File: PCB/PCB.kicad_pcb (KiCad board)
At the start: 2 copper layers, 120 x 60 mm, 63 parts, among them J1 USB_C_Receptacle_USB2.0_16P, J2 Conn_01x15, J3 Conn_01x15, Q2 IRLML2060, SW1 TSA016A2526B, SW2 TSA016A2526B, SW3 TSA016A2526B, U1 RP2040, U2 USBLC6-2SC6, U3 NCP1117ST33T3G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

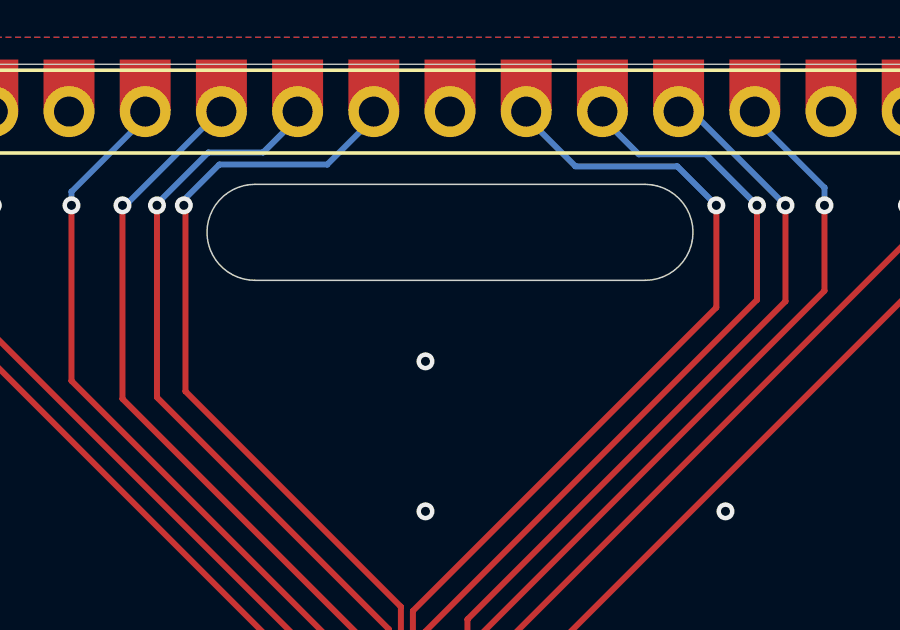
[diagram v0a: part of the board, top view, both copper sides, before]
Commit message: new mounting hole
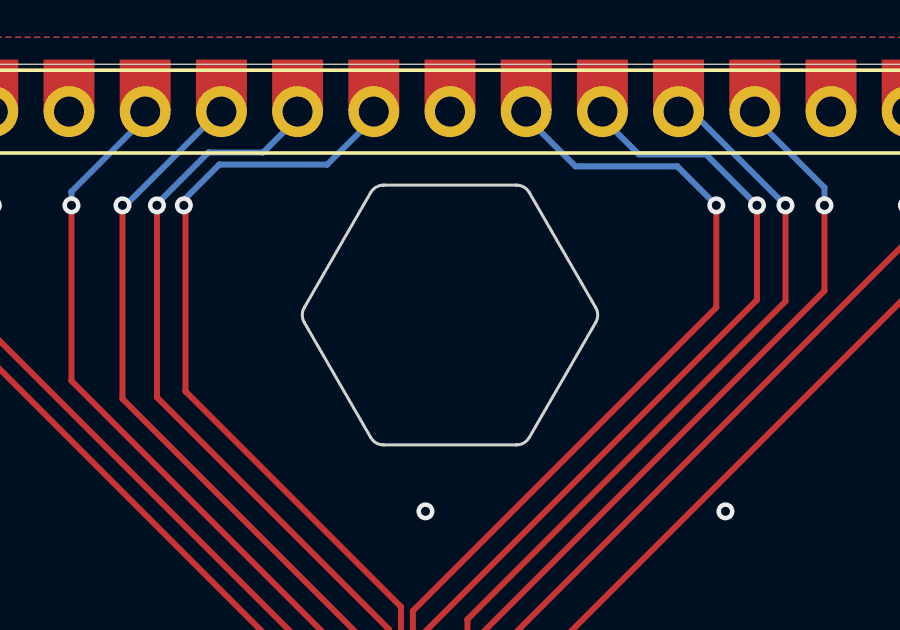
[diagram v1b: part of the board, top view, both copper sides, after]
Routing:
- net GND: vias 112 -> 111
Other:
- outline, holes or cut-outs redrawn
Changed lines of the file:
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@@
 			)
 		)
+		(model "/home/kai/Downloads/2-9in-e-ink-display-red-black-1.snapshot.11/Waveshare 2.9 (B) E-ink - Display Folded Flush.stp"
+			(offset
+				(xyz 0 28 1.5)
+			)
+			(scale
+				(xyz 1 1 1)
+			)
+			(rotate
+				(xyz -0 -0 -90)
+			)
+		)
 	)
 	(footprint "Capacitor_SMD:C_0402_1005Metric"
@@
 		(layer "Dwgs.User")
 	)
-	(gr_arc
-		(start 147.317629 29.1)
-		(mid 148.9176 30.7)
-		(end 147.317629 32.3)
+	(gr_line
+		(start 138.173261 29.374999)
+		(end 135.961936 33.205129)
 		(stroke
-			(width 0.05)
+			(width 0.1)
 			(type default)
 		)
@@
 		(layer "Edge.Cuts")
 	)
+	(gr_arc
+		(start 138.173261 29.374999)
+		(mid 138.356274 29.191987)
+		(end 138.606273 29.125)
+		(stroke
+			(width 0.1)
+			(type default)
+		)
+		(layer "Edge.Cuts")
+	)
 	(gr_line
-		(start 134.317629 32.3)
-		(end 147.317629 32.3)
+		(start 138.606273 37.785254)
+		(end 143.028909 37.785254)
 		(stroke
-			(width 0.05)
+			(width 0.1)
 			(type default)
 		)
@@
 	)
 	(gr_arc
+		(start 135.961936 33.705125)
+		(mid 135.894949 33.455127)
+		(end 135.961936 33.205129)
+		(stroke
+			(width 0.1)
+			(type default)
+		)
+		(layer "Edge.Cuts")
+	)
+	(gr_arc
+		(start 145.673265 33.205134)
+		(mid 145.740251 33.45513)
+		(end 145.673262 33.705125)
+		(stroke
+			(width 0.1)
+			(type default)
+		)
+		(layer "Edge.Cuts")
+	)
+	(gr_arc
+		(start 138.606273 37.785254)
+		(mid 138.356273 37.718267)
+		(end 138.173261 37.535254)
+		(stroke
+			(width 0.1)
+			(type default)
+		)
+		(layer "Edge.Cuts")
+	)
+	(gr_arc
 		(start 192.55414 85.097818)
 		(mid 192.210306 84.96078)
@@
 		(layer "Edge.Cuts")
 	)
+	(gr_line
+		(start 143.028939 29.125)
+		(end 138.606273 29.125)
+		(stroke
+			(width 0.1)
+			(type default)
+		)
+		(layer "Edge.Cuts")
+	)
+	(gr_arc
+		(start 143.461944 37.535243)
+		(mid 143.278922 37.718265)
+		(end 143.028909 37.785254)
+		(stroke
+			(width 0.1)
+			(type default)
+		)
+		(layer "Edge.Cuts")
+	)
+	(gr_line
+		(start 143.461944 37.535243)
+		(end 145.673262 33.705125)
+		(stroke
+			(width 0.1)
+			(type default)
+		)
+		(layer "Edge.Cuts")
+	)
 	(gr_arc
 		(start 192.054848 25.570791)
@@
 	)
 	(gr_line
-		(start 192.558935 25.097818)
-		(end 209.08114 25.097818)
+		(start 145.673265 33.205134)
+		(end 143.461932 29.374991)
 		(stroke
-			(width 0.01)
+			(width 0.1)
 			(type default)
 		)
@@
 	)
 	(gr_line
-		(start 192.55414 85.097818)
-		(end 209.08583 85.097818)
+		(start 192.558935 25.097818)
+		(end 209.08114 25.097818)
 		(stroke
 			(width 0.01)
@@
 		(layer "Edge.Cuts")
 	)
-	(gr_arc
-		(start 134.317629 32.3)
-		(mid 132.7176 30.7)
-		(end 134.317629 29.1)
+	(gr_line
+		(start 192.55414 85.097818)
+		(end 209.08583 85.097818)
 		(stroke
-			(width 0.05)
+			(width 0.01)
 			(type default)
 		)
@@
 	)
 	(gr_line
-		(start 147.317629 29.1)
-		(end 134.317629 29.1)
+		(start 135.961936 33.705125)
+		(end 138.173261 37.535254)
 		(stroke
-			(width 0.05)
+			(width 0.1)
 			(type default)
 		)
@@
 		(layer "Edge.Cuts")
 	)
+	(gr_arc
+		(start 143.028939 29.125)
+		(mid 143.278929 29.191985)
+		(end 143.461932 29.374991)
+		(stroke
+			(width 0.1)
+			(type default)
+		)
+		(layer "Edge.Cuts")
+	)
 	(gr_text "Some sketchy ground stuff, but I wanted it symmetrical and also a nice no-fill"
 		(at 186 23 0)
@@
 	)
 	(via
-		(at 140 35)
-		(size 0.6)
-		(drill 0.3)
-		(layers "F.Cu" "B.Cu")
-		(free yes)
-		(net 2)
-	)
-	(via
 		(at 140.65 48.2)
 		(size 0.6)
@@
 	)
 	(group ""
-		(members "162ab123-923f-4e19-be61-0324decd1f67" "1efb17f0-22fb-40ea-8807-f4fe69c3b792"
-			"b7a0f540-713e-4c9b-964d-49741287ba49" "b864c2af-c021-4858-a3a0-57c0e8108585"
+		(members "0ce7d37b-55d1-42f5-b13d-9c9e3b05c39b" "1f2a5adc-6555-4ce7-a0a5-fbe4a5895658"
+			"2173a039-1b9a-4af3-a71f-11988ef09e77" "54306ec1-47c2-4ec0-9eab-b388f6fdc17e"
+			"5c52c278-44df-4e44-92cc-903473877560" "62448e19-7cc3-44b4-a87d-d9a49ac190a5"
+			"762d25f0-1da9-4a48-9eb9-bc840d037b1e" "8121fe78-a763-4337-866c-79c3fbb7839a"
+			"90dd8e04-e499-4d71-acf3-162c82c6a650" "a5d14ade-53ac-40ed-b384-6d3397fe894e"
+			"b7da73b2-b1ba-4571-aaf0-42c2c0c642ad" "f407a7cb-ce11-4b17-9b3c-b1eebdf68950"
 		)
 	)

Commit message: new fab filess with changes
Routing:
- net /GPIO24: track 32.3 -> 27.8 mm
- net /GPIO23: track 33.6 -> 30.1 mm
- net /GPIO25: track 30.9 -> 28.2 mm
- net /GPIO22: track 32.8 -> 30.4 mm
- net /GPIO26: track 29.7 -> 28.6 mm
- net +3V3: track 256.5 -> 255.9 mm
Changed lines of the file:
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@@
 			)
 			(rotate
-				(xyz -0 -0 -90)
+				(xyz -0 -0 90)
 			)
 		)
@@
 	)
 	(segment
+		(start 151.2 29.8)
+		(end 151.2 33.8)
+		(width 0.2)
+		(layer "F.Cu")
+		(net 3)
+	)
+	(segment
 		(start 136.478778 54.340998)
 		(end 135.943504 54.340998)
@@
 	)
 	(segment
-		(start 152 29.9)
-		(end 152 33)
-		(width 0.2)
-		(layer "F.Cu")
-		(net 3)
-	)
-	(segment
 		(start 122.021004 48.19)
 		(end 123.881004 50.05)
@@
 	)
 	(segment
-		(start 152 33)
+		(start 151.2 33.8)
 		(end 141.399 43.601)
 		(width 0.2)
@@
 	)
 	(via
-		(at 152 29.8)
+		(at 151.2 29.8)
 		(size 0.6)
 		(drill 0.3)
@@
 	)
 	(segment
+		(start 149.087795 26.887795)
+		(end 148.437629 26.887795)
+		(width 0.2)
+		(layer "B.Cu")
+		(net 3)
+	)
+	(segment
 		(start 140.415533 45.534467)
 		(end 143.934467 45.534467)
@@
 	)
 	(segment
+		(start 151.2 29.8)
+		(end 151.2 29)
+		(width 0.2)
+		(layer "B.Cu")
+		(net 3)
+	)
+	(segment
+		(start 151.2 29)
+		(end 149.087795 26.887795)
+		(width 0.2)
+		(layer "B.Cu")
+		(net 3)
+	)
+	(segment
 		(start 161.271004 54.535577)
 		(end 162.083891 53.72269)
@@
 	)
 	(segment
-		(start 152 29.9)
-		(end 152 29.8)
-		(width 0.2)
-		(layer "B.Cu")
-		(net 3)
-	)
-	(segment
 		(start 143.5 63.8)
 		(end 143.5 67.2)
@@
 	)
 	(segment
-		(start 152 29.8)
-		(end 149.087795 26.887795)
-		(width 0.2)
-		(layer "B.Cu")
-		(net 3)
-	)
-	(segment
 		(start 133.199974 83.307795)
 		(end 133.199974 80.700026)
@@
 	)
 	(segment
-		(start 149.087795 26.887795)
-		(end 148.437629 26.887795)
-		(width 0.2)
-		(layer "B.Cu")
-		(net 3)
-	)
-	(segment
 		(start 199.275 72.725)
 		(end 204.275 77.725)
@@
 	)
 	(segment
-		(start 132 36)
-		(end 132 29.854315)
+		(start 135 30.8)
+		(end 136 29.8)
 		(width 0.2)
 		(layer "F.Cu")
@@
 	)
 	(segment
-		(start 132 29.854315)
-		(end 131.945685 29.8)
+		(start 135 39)
+		(end 135 30.8)
 		(width 0.2)
 		(layer "F.Cu")
@@
 	(segment
 		(start 139.181004 43.181004)
-		(end 132 36)
+		(end 135 39)
 		(width 0.2)
 		(layer "F.Cu")
@@
 	)
 	(via
-		(at 131.945685 29.8)
+		(at 136 29.8)
 		(size 0.6)
 		(drill 0.3)
@@
 	)
 	(segment
-		(start 133.127305 28.439795)
-		(end 136.725629 28.439795)
+		(start 138.4 27.4)
+		(end 138.4 27.010166)
 		(width 0.2)
 		(layer "B.Cu")
@@
 	)
 	(segment
-		(start 136.725629 28.439795)
+		(start 138.4 27.010166)
 		(end 138.277629 26.887795)
 		(width 0.2)
@@
 	)
 	(segment
-		(start 131.945685 29.621415)
-		(end 133.127305 28.439795)
-		(width 0.2)
-		(layer "B.Cu")
-		(net 47)
-	)
-	(segment
-		(start 131.945685 29.8)
-		(end 131.945685 29.621415)
+		(start 136 29.8)
+		(end 138.4 27.4)
 		(width 0.2)
 		(layer "B.Cu")
@@
 	)
 	(segment
-		(start 151.05 32.95)
-		(end 139.981004 44.018996)
+		(start 139.981004 44.018996)
+		(end 139.981004 51.503498)
 		(width 0.2)
 		(layer "F.Cu")
@@
 	)
 	(segment
-		(start 139.981004 44.018996)
-		(end 139.981004 51.503498)
+		(start 149.4 29.8)
+		(end 149.4 34.6)
 		(width 0.2)
 		(layer "F.Cu")
@@
 	)
 	(segment
-		(start 151.05 29.8)
-		(end 151.05 32.95)
+		(start 149.4 34.6)
+		(end 139.981004 44.018996)
 		(width 0.2)
 		(layer "F.Cu")
@@
 	)
 	(via
-		(at 151.05 29.8)
+		(at 149.4 29.8)
 		(size 0.6)
 		(drill 0.3)
@@
 	)
 	(segment
-		(start 151.05 29.8)
-		(end 149.349 28.099)
-		(width 0.2)
-		(layer "B.Cu")
-		(net 51)
-	)
-	(segment
-		(start 149.349 28.099)
-		(end 147.108834 28.099)
-		(width 0.2)
-		(layer "B.Cu")
-		(net 51)
-	)
-	(segment
-		(start 151.05 30)
-		(end 151.05 29.8)
+		(start 146.275 26.675)
+		(end 149.4 29.8)
 		(width 0.2)
 		(layer "B.Cu")
@@
 	)
 	(segment
-		(start 147.108834 28.099)
-		(end 145.897629 26.887795)
+		(start 145.897629 26.675)
+		(end 146.275 26.675)
 		(width 0.2)
 		(layer "B.Cu")
@@
 	)
 	(segment
-		(start 131.05 36.2)
+		(start 133.4 38.55)
 		(end 138.781004 43.931004)
 		(width 0.2)
@@
 	)
 	(segment
-		(start 138.781004 43.931004)
-		(end 138.781004 51.503498)
+		(start 133.4 29.8)
+		(end 133.4 38.55)
 		(width 0.2)
 		(layer "F.Cu")
@@
 	)
 	(segment
-		(start 131.05 29.75)
-		(end 131.05 36.2)
+		(start 138.781004 43.931004)
+		(end 138.781004 51.503498)
 		(width 0.2)
 		(layer "F.Cu")
@@
 	)
 	(via
-		(at 131.05 29.8)
+		(at 133.4 29.8)
 		(size 0.6)
 		(drill 0.3)
@@
 	)
 	(segment
-		(start 134.586629 28.038795)
-		(end 135.737629 26.887795)
-		(width 0.2)
-		(layer "B.Cu")
-		(net 52)
-	)
-	(segment
-		(start 131.05 29.8)
-		(end 131.05 29.75)
+		(start 135.737629 27.462371)
+		(end 135.737629 26.675)
 		(width 0.2)
 		(layer "B.Cu")
@@
 	)
 	(segment
-		(start 131.05 29.75)
-		(end 132.761205 28.038795)
+		(start 133.4 29.8)
+		(end 135.737629 27.462371)
 		(width 0.2)
 		(layer "B.Cu")
@@
 	)
 	(segment
-		(start 132.761205 28.038795)
-		(end 134.586629 28.038795)
+		(start 135.737629 26.675)
+		(end 135.737629 26.887795)
 		(width 0.2)
 		(layer "B.Cu")
@@
 	)
 	(segment
-		(start 139.581004 51.503498)
+		(start 147.2 35.7)
 		(end 139.581004 43.318996)
 		(width 0.2)
@@
 	)
 	(segment
-		(start 149.695243 33.204757)
-		(end 149.695243 29.8)
+		(start 147.2 29.8)
+		(end 147.2 35.7)
 		(width 0.2)
 		(layer "F.Cu")
@@
 	(segment
 		(start 139.581004 43.318996)
-		(end 149.695243 33.204757)
+		(end 139.581004 51.503498)
 		(width 0.2)
 		(layer "F.Cu")
@@
 	)
 	(via
-		(at 149.695243 29.8)
+		(at 147.2 29.8)
 		(size 0.6)
 		(drill 0.3)
@@
 	)
 	(segment
-		(start 148.395243 28.5)
-		(end 145 28.5)
-		(width 0.2)
-		(layer "B.Cu")
-		(net 57)
-	)
-	(segment
-		(start 145 28.5)
-		(end 143.387795 26.887795)
-		(width 0.2)
-		(layer "B.Cu")
-		(net 57)
-	)
-	(segment
-		(start 149.695243 29.8)
-		(end 148.395243 28.5)
+		(start 147.345243 29.945243)
+		(end 147.2 29.8)
 		(width 0.2)
 		(layer "B.Cu")
@@
 	)
 	(segment
-		(start 149.695243 29.945243)
-		(end 149.695243 29.8)
+		(start 144.287795 26.887795)
+		(end 143.357629 26.887795)
 		(width 0.2)
 		(layer "B.Cu")
@@
 	)
 	(segment
-		(start 143.387795 26.887795)
-		(end 143.357629 26.887795)
+		(start 147.2 29.8)
+		(end 144.287795 26.887795)
 		(width 0.2)
 		(layer "B.Cu")
@@
 	)
 	(segment
-		(start 129.9 36.25)
+		(start 131.2 37.55)
 		(end 138.381004 44.731004)
 		(width 0.2)
@@
 	)
 	(segment
-		(start 129.9 29.8)
-		(end 129.9 36.25)
+		(start 131.2 29.8)
+		(end 131.2 37.55)
 		(width 0.2)
 		(layer "F.Cu")
@@
 	)
 	(via
-		(at 129.9 29.8)
+		(at 131.2 29.8)
 		(size 0.6)
 		(drill 0.3)
@@
 	)
 	(segment
-		(start 129.9 29.8)
-		(end 130 29.8)
+		(start 131.2 28.6)
+		(end 132.912205 26.887795)
 		(width 0.2)
 		(layer "B.Cu")
@@
 	)
 	(segment
-		(start 132.912205 26.887795)
-		(end 133.197629 26.887795)
+		(start 131.2 29.8)
+		(end 131.2 28.6)
 		(width 0.2)
 		(layer "B.Cu")
@@
 	)
 	(segment
-		(start 130 29.8)
-		(end 132.912205 26.887795)
+		(start 132.912205 26.887795)
+		(end 133.197629 26.887795)
 		(width 0.2)
 		(layer "B.Cu")

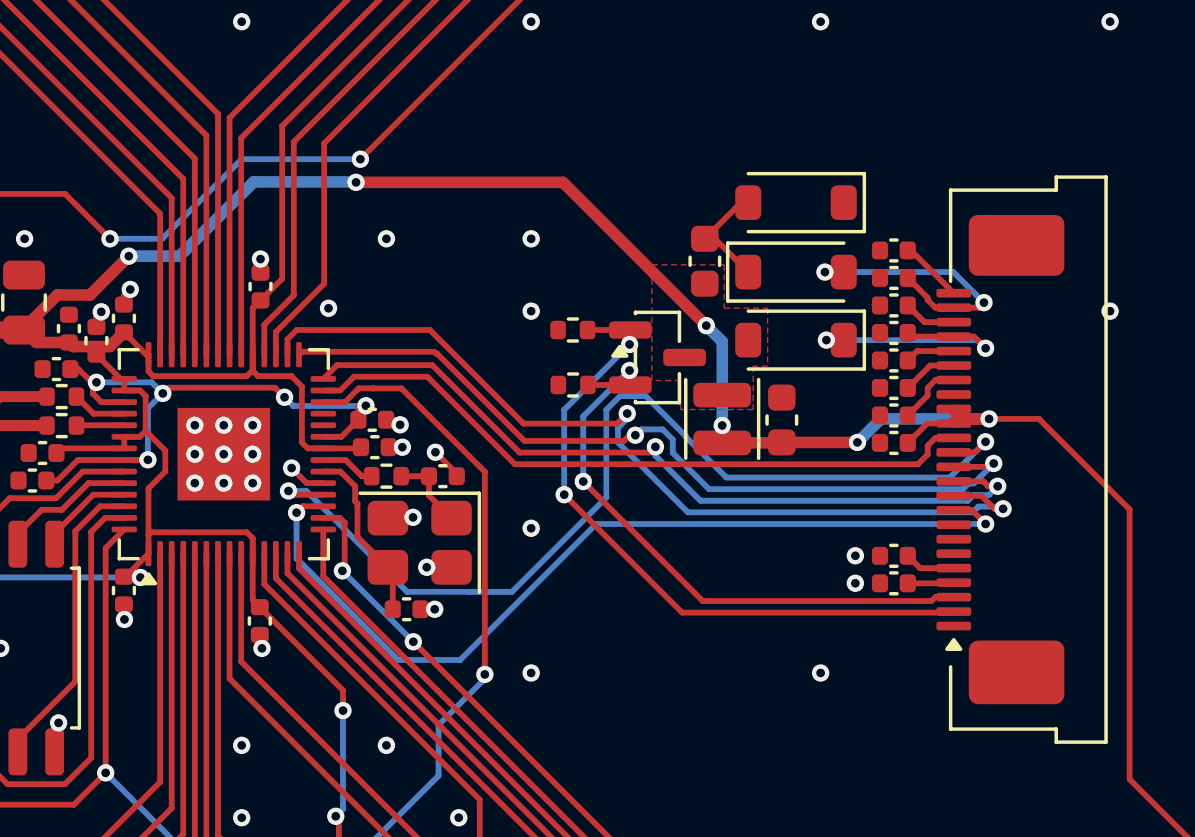
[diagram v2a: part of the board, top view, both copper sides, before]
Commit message: actually decided on this inductor!
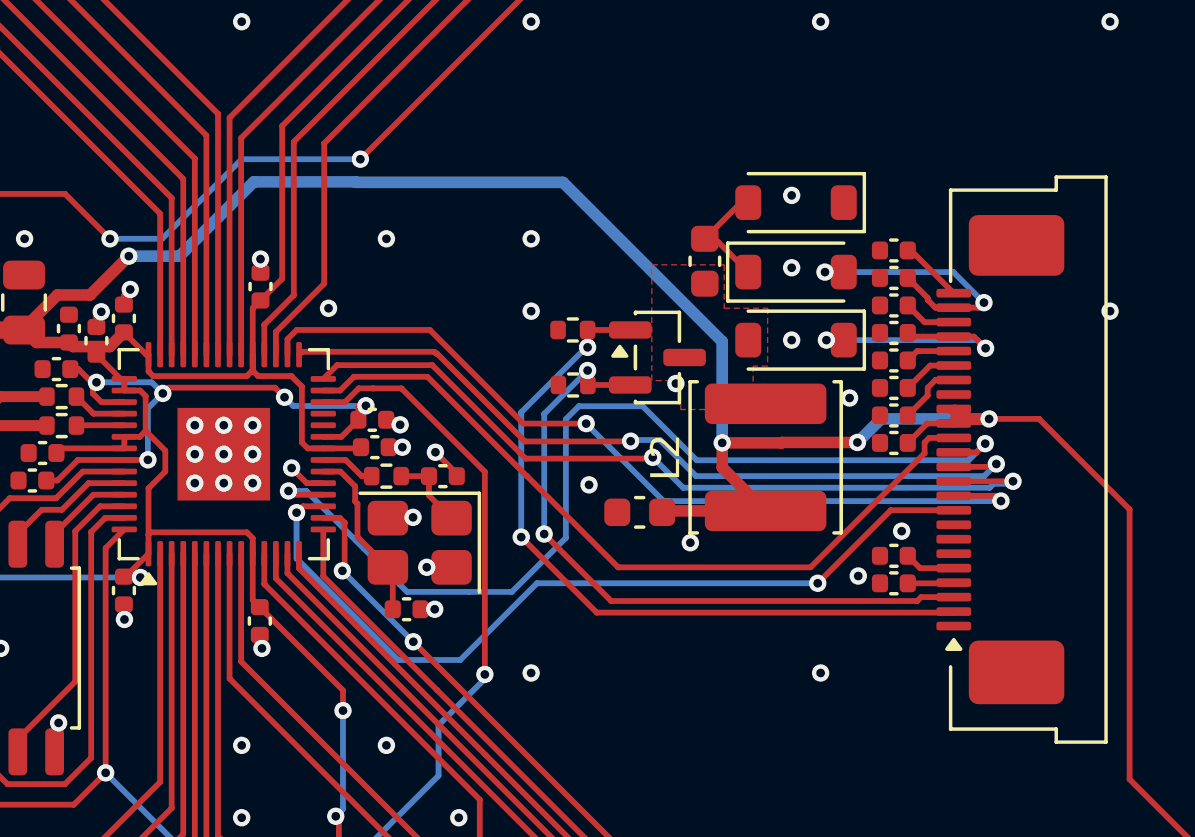
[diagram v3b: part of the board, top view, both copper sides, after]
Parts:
- L2: footprint Inductor_SMD:L_Sunlord_SWPA252010S -> Inductor_SMD:L_Sunlord_SWPA5020S
- moved C28 5.86 mm to (153.8, 57.0), turned to 0 degrees
- moved L2 2.00 mm to (158.1, 55.0)
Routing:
- net +3V3: track 255.9 -> 262.4 mm, vias 16 -> 14
- net /EPD_MOSI: track 23.8 -> 26.8 mm
- net /GDR: track 23.3 -> 25.6 mm
- net /RESE: track 21.0 -> 23.4 mm
- net /EPD_BUSY: track 31.1 -> 28.9 mm
- net /EPD_RST: track 31.3 -> 29.5 mm
- net /EPD_CS: track 28.4 -> 27.6 mm
- net GND: vias 111 -> 117

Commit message: finishing touches, new fab files!
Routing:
- net GND: vias 117 -> 124
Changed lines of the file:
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@@
+	)
+	(via
+		(at 145 72)
+		(size 0.6)
+		(drill 0.3)
+		(layers "F.Cu" "B.Cu")
+		(free yes)
+		(net 2)
 	)
 	(via
@@
 	)
 	(via
+		(at 136 73)
+		(size 0.6)
+		(drill 0.3)
+		(layers "F.Cu" "B.Cu")
+		(free yes)
+		(net 2)
+	)
+	(via
 		(at 130 70)
 		(size 0.6)
@@
 	)
 	(via
-		(at 131.675 61.65)
+		(at 132.425 62.4)
 		(size 0.6)
 		(drill 0.3)
@@
 	)
 	(via
+		(at 116.5 50)
+		(size 0.6)
+		(drill 0.3)
+		(layers "F.Cu" "B.Cu")
+		(free yes)
+		(net 2)
+	)
+	(via
+		(at 130.925 62.4)
+		(size 0.6)
+		(drill 0.3)
+		(layers "F.Cu" "B.Cu")
+		(free yes)
+		(net 2)
+	)
+	(via
 		(at 182 70)
 		(size 0.6)
@@
 	)
 	(via
+		(at 155 46)
+		(size 0.6)
+		(drill 0.3)
+		(layers "F.Cu" "B.Cu")
+		(free yes)
+		(net 2)
+	)
+	(via
 		(at 186.35 50.05)
 		(size 0.6)
@@
 	)
 	(via
+		(at 132.425 60.9)
+		(size 0.6)
+		(drill 0.3)
+		(layers "F.Cu" "B.Cu")
+		(free yes)
+		(net 2)
+	)
+	(via
 		(at 155.5 58)
 		(size 0.6)
@@
 		(net 2)
 	)
+	(via
+		(at 130.925 60.9)
+		(size 0.6)
+		(drill 0.3)
+		(layers "F.Cu" "B.Cu")
+		(free yes)
+		(net 2)
+	)
